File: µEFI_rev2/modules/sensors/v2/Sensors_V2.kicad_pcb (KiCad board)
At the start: 2 copper layers, 15.2 x 11.2 mm, 12 parts, among them J1 Conn_01x05_Female, U1 LM321, U2 LM321

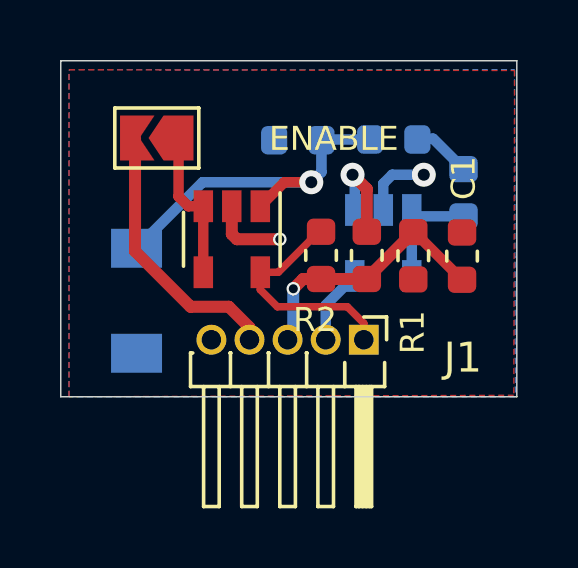
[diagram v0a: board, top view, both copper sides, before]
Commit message: Making sensor board easier to assemble
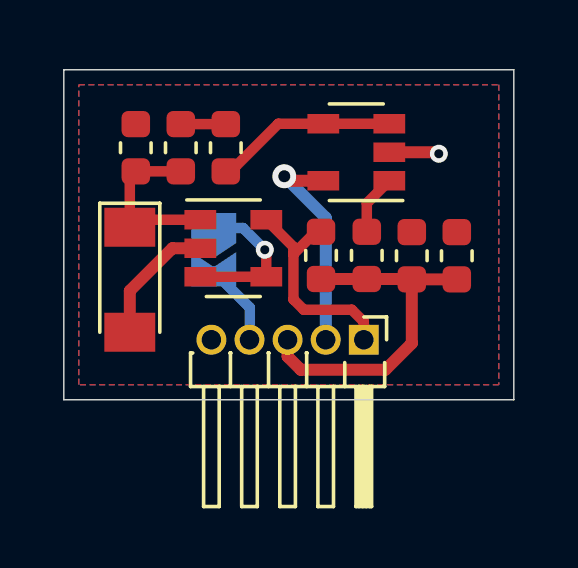
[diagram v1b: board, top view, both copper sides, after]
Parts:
- D1, R4, R5, R6, U1: moved to F.Cu
- JP1: moved to B.Cu
- moved R4 8.07 mm to (140.4, 79.6)
- moved R5 7.11 mm to (138.9, 79.6), turned to 90 degrees
- moved R6 5.41 mm to (137.4, 79.6), turned to 90 degrees
- moved JP1 4.18 mm to (140.0, 83.0), turned to -90 degrees
- moved U1 3.16 mm to (144.8, 79.8), turned to 180 degrees
- moved D1 0.74 mm to (137.2, 84.0)
- moved U2 0.30 mm to (140.7, 83.0), turned to 0 degrees
- moved C1 0.18 mm to (148.1, 83.2)
- moved R1 0.05 mm to (146.6, 83.2), turned to 90 degrees
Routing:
- net (no net): track 33.2 -> 0.00 mm
- net Net-(D1-Pad1): track 12.2 -> 5.90 mm, vias 1 -> 0
- net Net-(J1-Pad4): track 9.05 -> 2.78 mm
- net +12V: track 2.53 -> 7.38 mm, vias 0 -> 1
- net /IN: track 8.91 -> 11.9 mm, vias 1 -> 0
- net Net-(R4-Pad1): track 4.01 -> 6.11 mm
- net Net-(R3-Pad1): track 3.30 -> 2.01 mm, vias 1 -> 0
- net GND: track 4.95 -> 5.99 mm, vias 2 -> 1
- net Net-(JP1-Pad1): track 5.11 -> 5.12 mm, vias 0 -> 1
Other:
- board size 15.2 x 11.2 mm -> 15 x 11 mm
- board text added: "EN"
- board text removed: "ENABLE"
